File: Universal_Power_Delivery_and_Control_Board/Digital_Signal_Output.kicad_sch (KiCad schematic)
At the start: 14 parts, among them U15 SN74LVC541APWR_C113281, U16 SN74LVC541APWR_C113281

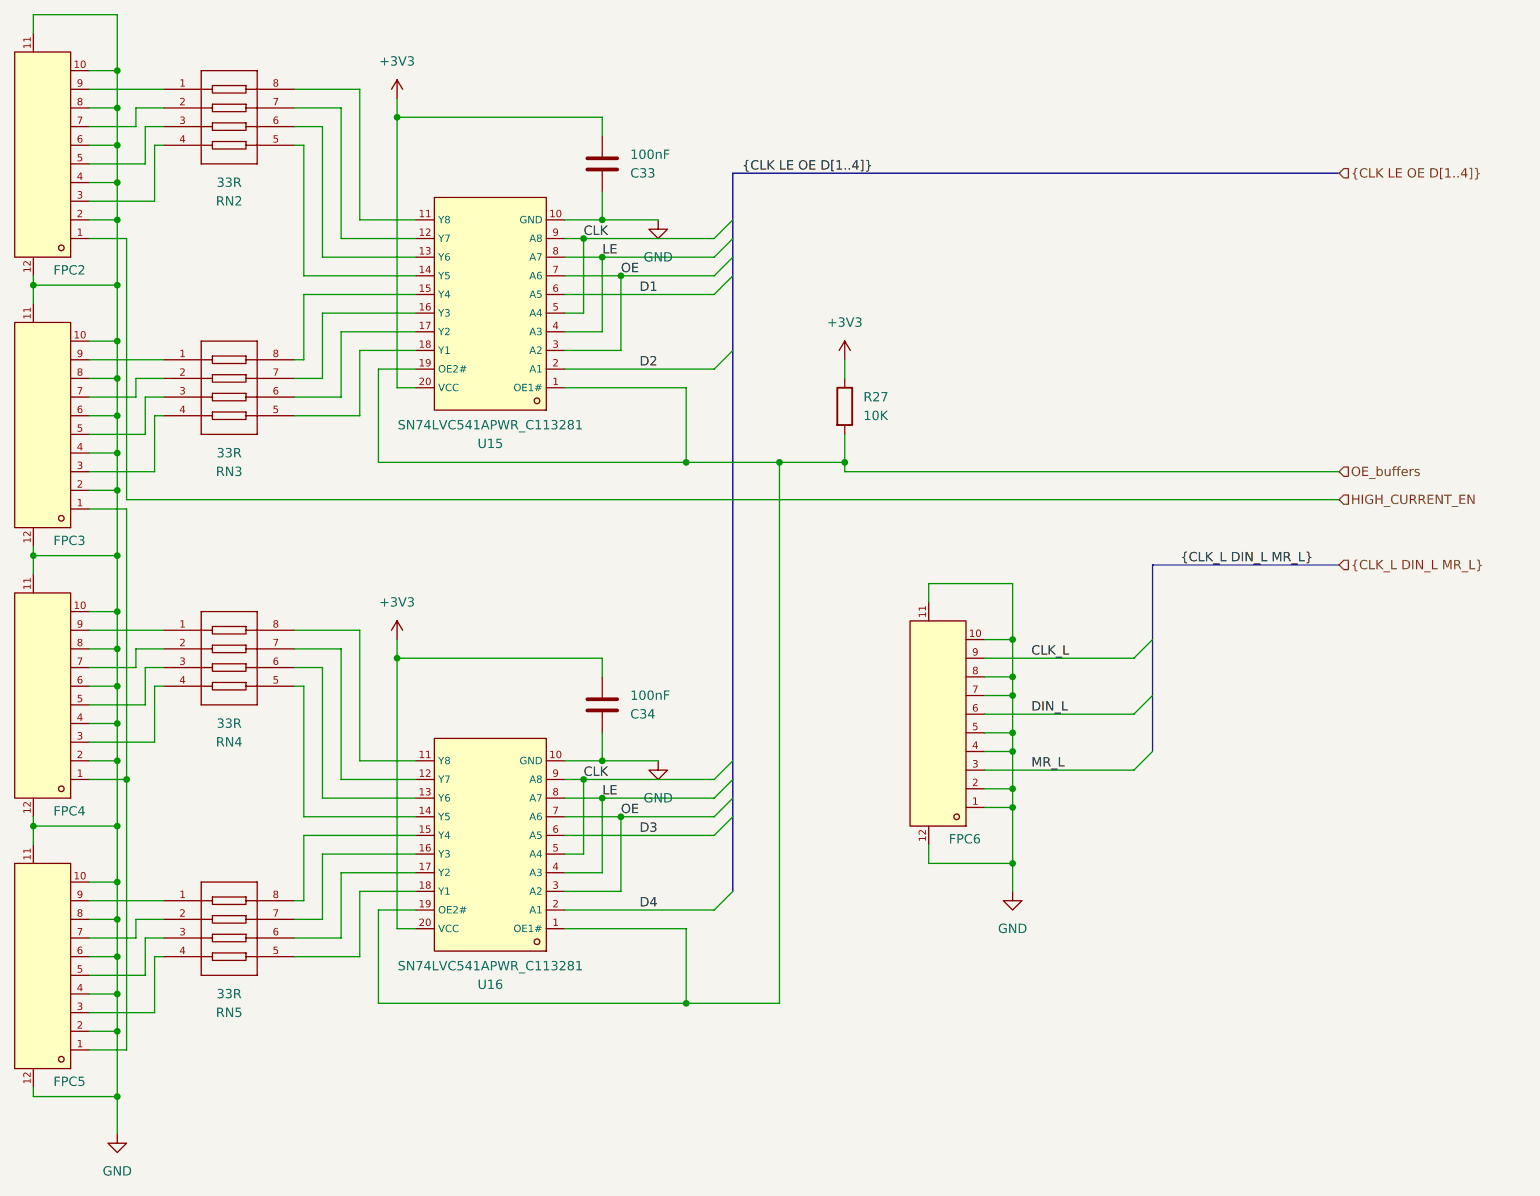
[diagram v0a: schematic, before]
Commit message: Switched to a 4 layer stackup and routed the digital output section.
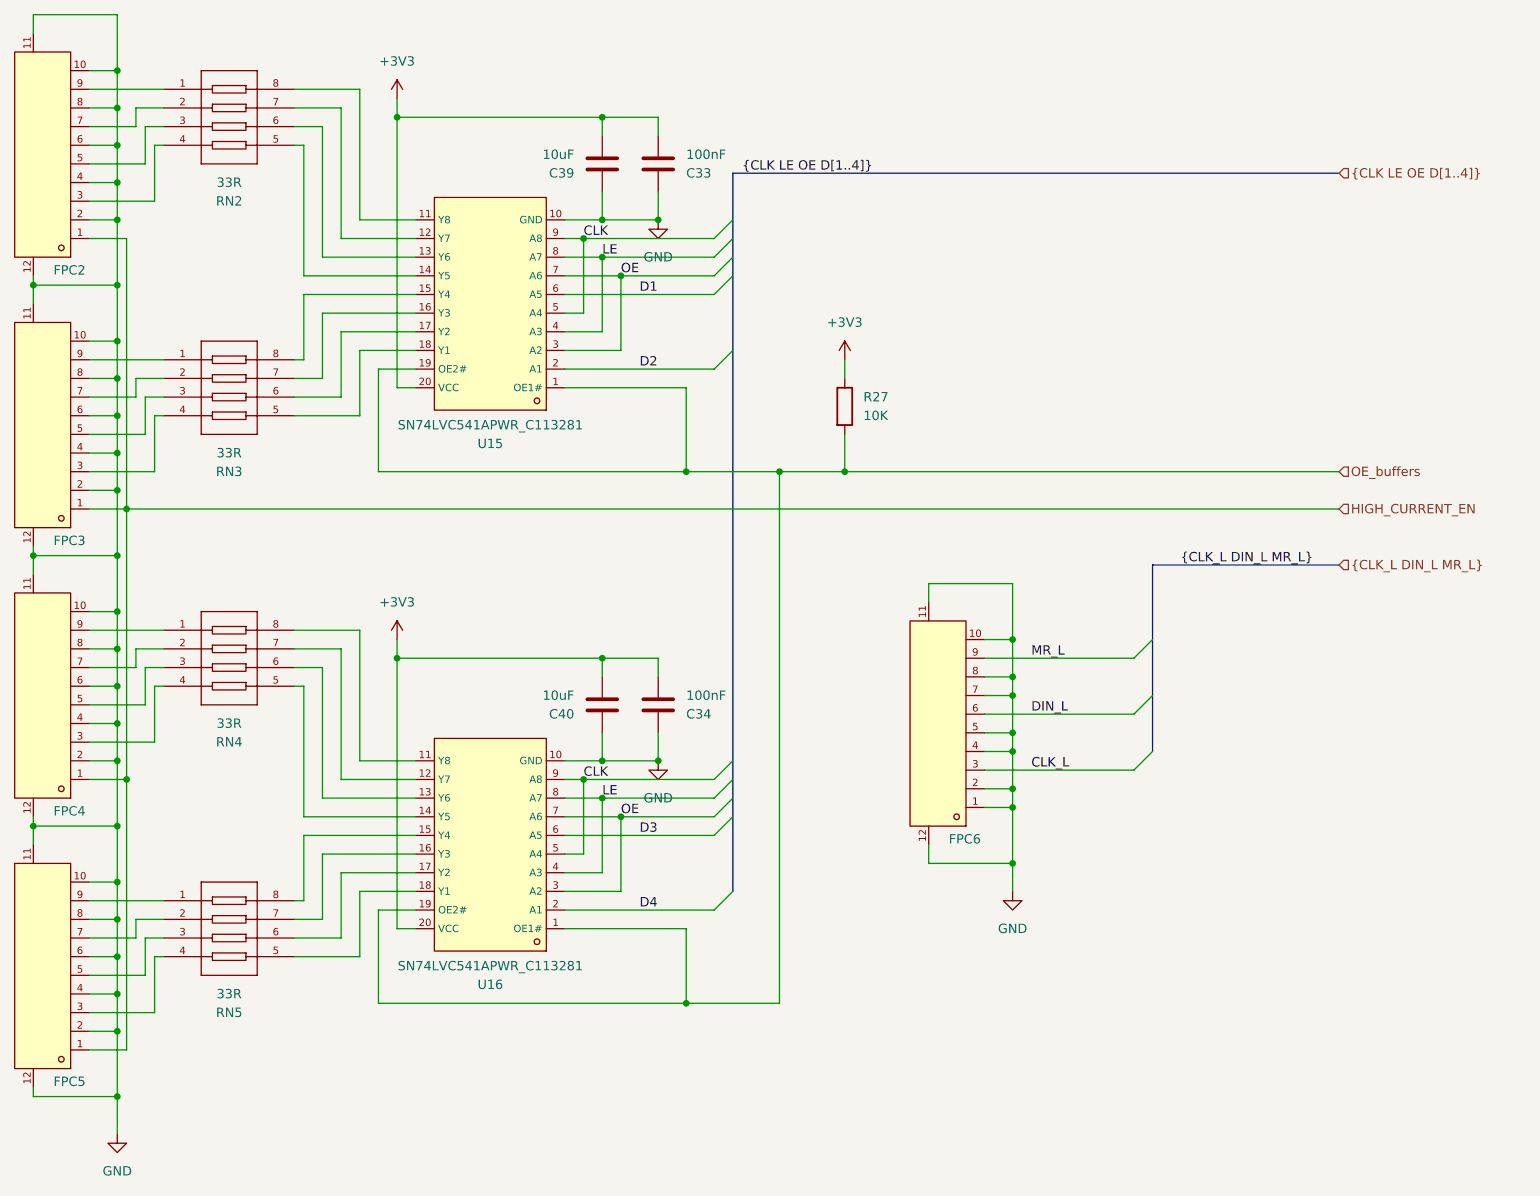
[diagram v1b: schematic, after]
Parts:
- added C39, C40: 10uF, Capacitor_SMD:C_0805_2012Metric_Pad1.18x1.45mm_HandSolder, symbol Device:C
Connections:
- net +3V3: now also C39.2, C40.2
- net CLK_L: now also FPC6.3; no longer FPC6.9
- net GND: now also C39.1, C40.1
- net HIGH_CURRENT_EN: now also FPC3.1, FPC4.1, FPC5.1
- net MR_L: now also FPC6.9; no longer FPC6.3
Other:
- moved on the sheet: C33, C34

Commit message: Small mostly cosmetic changes and reannotation of the schematic, followed by the export of the gerber files for production.
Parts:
- renumbered C39 to C45, C33 to C46, C40 to C47, C34 to C48, FPC6 to FPC5, FPC5 to FPC6, R27 to R41, U15 to U22, U16 to U23
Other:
- company: (none) -> Jan Ścibielski
- title: (none) -> Digital Signal Output
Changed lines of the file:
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@@
 	(generator_version "10.0")
 	(paper "A4")
+	(title_block
+		(title "Digital Signal Output")
+		(date "2026-08-15")
+		(rev "1.0")
+		(company "Jan Ścibielski")
+	)
 	(junction
 		(at 64.77 62.23)
@@
 		(in_pos_files yes)
 		(dnp no)
-		(property "Reference" "U15"
+		(property "Reference" "U22"
 			(at 115.57 83.82 0)
 			(show_name no)
@@
 			(project "Universal_Power_Delivery_and_Control_Board"
 				(path "/b749dd2f-6b66-411b-a989-65da6091f700/bdaed53d-5f4e-48c9-9e2a-f60b1b226061"
-					(reference "U15")
+					(reference "U22")
 					(unit 1)
 				)
@@
 		(dnp no)
 		(fields_autoplaced yes)
-		(property "Reference" "#PWR050"
+		(property "Reference" "#PWR082"
 			(at 102.87 40.64 0)
 			(hide yes)
@@
 			(project "Universal_Power_Delivery_and_Control_Board"
 				(path "/b749dd2f-6b66-411b-a989-65da6091f700/bdaed53d-5f4e-48c9-9e2a-f60b1b226061"
-					(reference "#PWR050")
+					(reference "#PWR082")
 					(unit 1)
 				)
@@
 		(dnp no)
 		(fields_autoplaced yes)
-		(property "Reference" "#PWR054"
+		(property "Reference" "#PWR085"
 			(at 102.87 114.3 0)
 			(hide yes)
@@
 			(project "Universal_Power_Delivery_and_Control_Board"
 				(path "/b749dd2f-6b66-411b-a989-65da6091f700/bdaed53d-5f4e-48c9-9e2a-f60b1b226061"
-					(reference "#PWR054")
+					(reference "#PWR085")
 					(unit 1)
 				)
@@
 		(dnp no)
 		(fields_autoplaced yes)
-		(property "Reference" "#PWR055"
+		(property "Reference" "#PWR086"
 			(at 138.43 133.35 0)
 			(hide yes)
@@
 			(project "Universal_Power_Delivery_and_Control_Board"
 				(path "/b749dd2f-6b66-411b-a989-65da6091f700/bdaed53d-5f4e-48c9-9e2a-f60b1b226061"
-					(reference "#PWR055")
+					(reference "#PWR086")
 					(unit 1)
 				)
@@
 		(in_pos_files yes)
 		(dnp no)
-		(property "Reference" "U16"
+		(property "Reference" "U23"
 			(at 115.57 157.48 0)
 			(show_name no)
@@
 			(project "Universal_Power_Delivery_and_Control_Board"
 				(path "/b749dd2f-6b66-411b-a989-65da6091f700/bdaed53d-5f4e-48c9-9e2a-f60b1b226061"
-					(reference "U16")
+					(reference "U23")
 					(unit 1)
 				)
@@
 		(in_pos_files yes)
 		(dnp no)
-		(property "Reference" "R27"
+		(property "Reference" "R41"
 			(at 166.37 77.4699 0)
 			(show_name no)
@@
 			(project "Universal_Power_Delivery_and_Control_Board"
 				(path "/b749dd2f-6b66-411b-a989-65da6091f700/bdaed53d-5f4e-48c9-9e2a-f60b1b226061"
-					(reference "R27")
+					(reference "R41")
 					(unit 1)
 				)
@@
 		(in_pos_files yes)
 		(dnp no)
-		(property "Reference" "C33"
+		(property "Reference" "C46"
 			(at 142.24 46.9901 0)
 			(show_name no)
@@
 			(project "Universal_Power_Delivery_and_Control_Board"
 				(path "/b749dd2f-6b66-411b-a989-65da6091f700/bdaed53d-5f4e-48c9-9e2a-f60b1b226061"
-					(reference "C33")
+					(reference "C46")
 					(unit 1)
 				)
@@
 		(in_pos_files yes)
 		(dnp no)
-		(property "Reference" "C40"
+		(property "Reference" "C47"
 			(at 127 120.6501 0)
 			(show_name no)
@@
 			(project "Universal_Power_Delivery_and_Control_Board"
 				(path "/b749dd2f-6b66-411b-a989-65da6091f700/bdaed53d-5f4e-48c9-9e2a-f60b1b226061"
-					(reference "C40")
+					(reference "C47")
 					(unit 1)
 				)
@@
 		(in_pos_files yes)
 		(dnp no)
-		(property "Reference" "FPC5"
+		(property "Reference" "FPC6"
 			(at 60.452 170.688 0)
 			(show_name no)
@@
 			(project "Universal_Power_Delivery_and_Control_Board"
 				(path "/b749dd2f-6b66-411b-a989-65da6091f700/bdaed53d-5f4e-48c9-9e2a-f60b1b226061"
-					(reference "FPC5")
+					(reference "FPC6")
 					(unit 1)
 				)
@@
 		(dnp no)
 		(fields_autoplaced yes)
-		(property "Reference" "#PWR057"
+		(property "Reference" "#PWR084"
 			(at 163.83 76.2 0)
 			(hide yes)
@@
 			(project "Universal_Power_Delivery_and_Control_Board"
 				(path "/b749dd2f-6b66-411b-a989-65da6091f700/bdaed53d-5f4e-48c9-9e2a-f60b1b226061"
-					(reference "#PWR057")
+					(reference "#PWR084")
 					(unit 1)
 				)
@@
 		(dnp no)
 		(fields_autoplaced yes)
-		(property "Reference" "#PWR056"
+		(property "Reference" "#PWR087"
 			(at 186.69 151.13 0)
 			(hide yes)
@@
 			(project "Universal_Power_Delivery_and_Control_Board"
 				(path "/b749dd2f-6b66-411b-a989-65da6091f700/bdaed53d-5f4e-48c9-9e2a-f60b1b226061"
-					(reference "#PWR056")
+					(reference "#PWR087")
 					(unit 1)
 				)
@@
 		(dnp no)
 		(fields_autoplaced yes)
-		(property "Reference" "#PWR047"
+		(property "Reference" "#PWR088"
 			(at 64.77 184.15 0)
 			(hide yes)
@@
 			(project "Universal_Power_Delivery_and_Control_Board"
 				(path "/b749dd2f-6b66-411b-a989-65da6091f700/bdaed53d-5f4e-48c9-9e2a-f60b1b226061"
-					(reference "#PWR047")
+					(reference "#PWR088")
 					(unit 1)
 				)
@@
 		(in_pos_files yes)
 		(dnp no)
-		(property "Reference" "FPC6"
+		(property "Reference" "FPC5"
 			(at 182.372 137.668 0)
 			(show_name no)
@@
 			(project "Universal_Power_Delivery_and_Control_Board"
 				(path "/b749dd2f-6b66-411b-a989-65da6091f700/bdaed53d-5f4e-48c9-9e2a-f60b1b226061"
-					(reference "FPC6")
+					(reference "FPC5")
 					(unit 1)
 				)
@@
 		(dnp no)
 		(fields_autoplaced yes)
-		(property "Reference" "#PWR053"
+		(property "Reference" "#PWR083"
 			(at 138.43 59.69 0)
 			(hide yes)
@@
 			(project "Universal_Power_Delivery_and_Control_Board"
 				(path "/b749dd2f-6b66-411b-a989-65da6091f700/bdaed53d-5f4e-48c9-9e2a-f60b1b226061"
-					(reference "#PWR053")
+					(reference "#PWR083")
 					(unit 1)
 				)
@@
 		(in_pos_files yes)
 		(dnp no)
-		(property "Reference" "C39"
+		(property "Reference" "C45"
 			(at 127 46.9901 0)
 			(show_name no)
@@
 			(project "Universal_Power_Delivery_and_Control_Board"
 				(path "/b749dd2f-6b66-411b-a989-65da6091f700/bdaed53d-5f4e-48c9-9e2a-f60b1b226061"
-					(reference "C39")
+					(reference "C45")
 					(unit 1)
 				)
@@
 		(in_pos_files yes)
 		(dnp no)
-		(property "Reference" "C34"
+		(property "Reference" "C48"
 			(at 142.24 120.6501 0)
 			(show_name no)
@@
 			(project "Universal_Power_Delivery_and_Control_Board"
 				(path "/b749dd2f-6b66-411b-a989-65da6091f700/bdaed53d-5f4e-48c9-9e2a-f60b1b226061"
-					(reference "C34")
+					(reference "C48")
 					(unit 1)
 				)
